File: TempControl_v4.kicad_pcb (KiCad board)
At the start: 2 copper layers, 57 x 38.1 mm, 42 parts, among them J1 LCD2, J2 PGM, J3 LCD1, J4 PWR, J5 Temp0, J6 Temp1, J7 AC, U1 PIC16(L)F88-I/P, U2 INA326, U3 INA326, U4 LM317_3PinPackage, U5 G3MB-202P

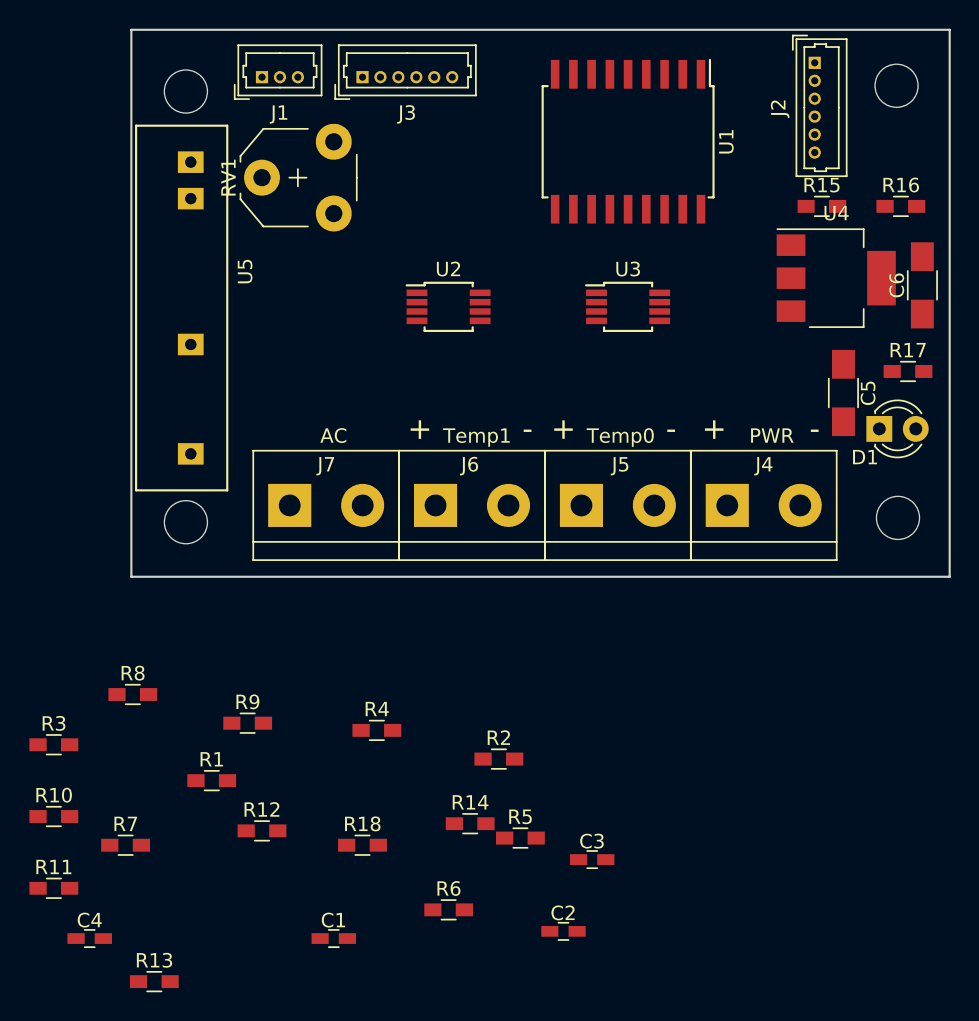
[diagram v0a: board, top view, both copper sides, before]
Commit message: Completed PCB layout
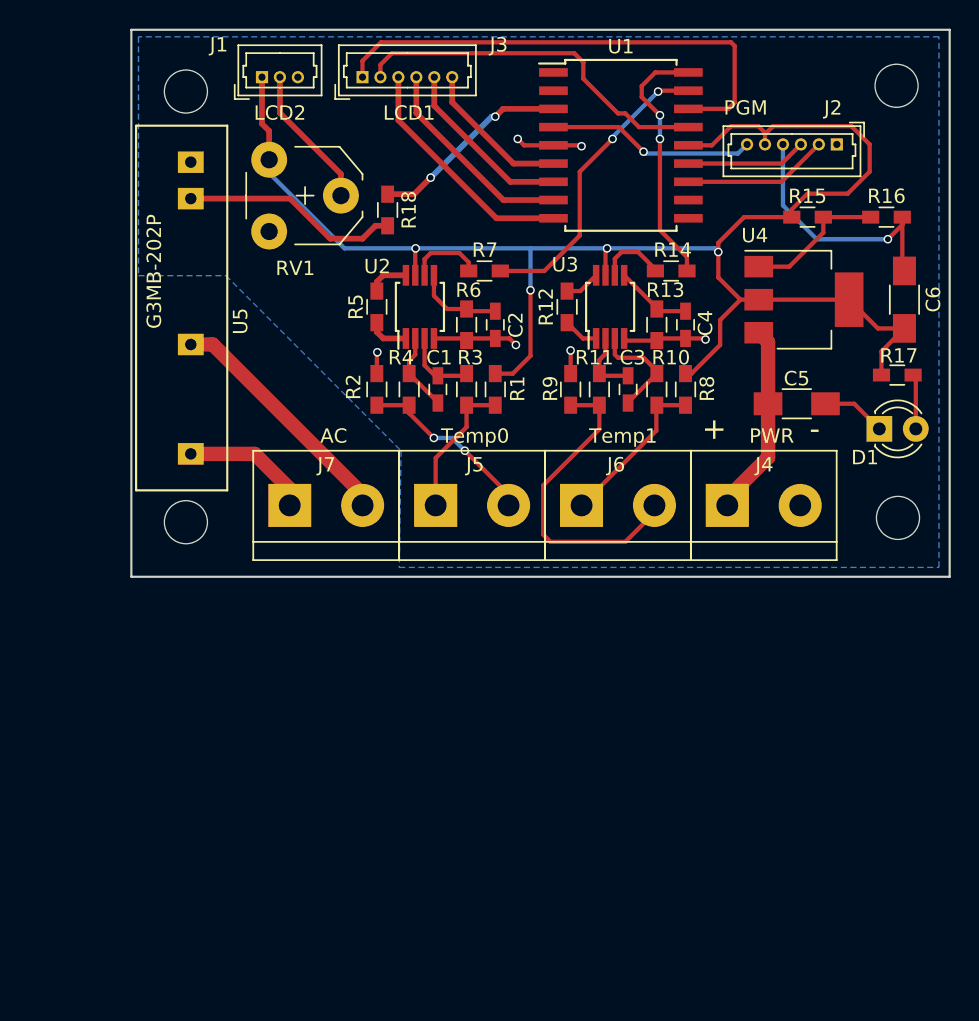
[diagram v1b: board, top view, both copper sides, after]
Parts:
- moved C4 59.6 mm to (166.5, 87.8), turned to 270 degrees
- moved R13 57.6 mm to (164.5, 87.8), turned to 270 degrees
- moved R11 51.5 mm to (160.5, 92.2), turned to 270 degrees
- moved R10 51.5 mm to (164.5, 92.2), turned to 270 degrees
- moved R7 47.2 mm to (152.5, 84.0), turned to 180 degrees
- moved R18 44.3 mm to (145.8, 79.8), turned to 90 degrees
- moved R8 44.0 mm to (166.5, 92.2), turned to 90 degrees
- moved C2 42.5 mm to (153.2, 87.8), turned to 270 degrees
- moved R12 42.2 mm to (158.2, 86.5), turned to 90 degrees
- moved R14 41.0 mm to (165.5, 84.0), turned to 180 degrees
- moved R6 40.8 mm to (151.2, 87.8), turned to 270 degrees
- moved C1 38.9 mm to (149.2, 92.2), turned to 270 degrees
- moved R5 38.3 mm to (145.0, 86.5), turned to 90 degrees
- moved R3 37.9 mm to (151.2, 92.2), turned to 270 degrees
- moved R1 33.7 mm to (153.2, 92.2), turned to 90 degrees
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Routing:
- net +5V: track 0.00 -> 112.2 mm, vias 0 -> 4
- net GND: track 0.00 -> 42.4 mm, vias 0 -> 7
- net Net-(J3-Pad1): track 0.00 -> 35.1 mm
- net Net-(J3-Pad2): track 0.00 -> 25.4 mm
- net /PT100_amp2/PT100_min: track 0.00 -> 21.9 mm
- net /PT100_amp/amp_out: track 0.00 -> 21.2 mm, vias 0 -> 2
- net /PT100_amp2/amp_out: track 0.00 -> 17.8 mm, vias 0 -> 2
- net /Relais/AC2_out: track 0.00 -> 17.1 mm
- net Net-(J3-Pad3): track 0.00 -> 16.6 mm
- net Net-(R18-Pad1): track 0.00 -> 15.2 mm
- net Net-(J3-Pad4): track 0.00 -> 14.6 mm
- net /PIC_VPP: track 0.00 -> 14.5 mm, vias 0 -> 1
- net /Power_supply/PWR_pos: track 0.00 -> 14.4 mm
- net /Relais/relais_trig: track 0.00 -> 14.0 mm, vias 0 -> 2
- net /PT100_amp/PT100_min: track 0.00 -> 13.1 mm, vias 0 -> 2
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- added copper zone on B.Cu, net GND
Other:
- net class Default: trace_width 0.25 -> 0.3
- net class High Voltage added: clearance 1.5, trace_width 1, via_dia 0.8, via_drill 0.6
- net class Power added: clearance 0.5, trace_width 1, via_dia 0.8, via_drill 0.6

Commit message: Added logo to PCB
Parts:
- added G***: LOGO, Graphics:Mountain_logo, B.Cu at (156.8, 82.2)
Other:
- board text added: "TempControl v4-Nov '17"

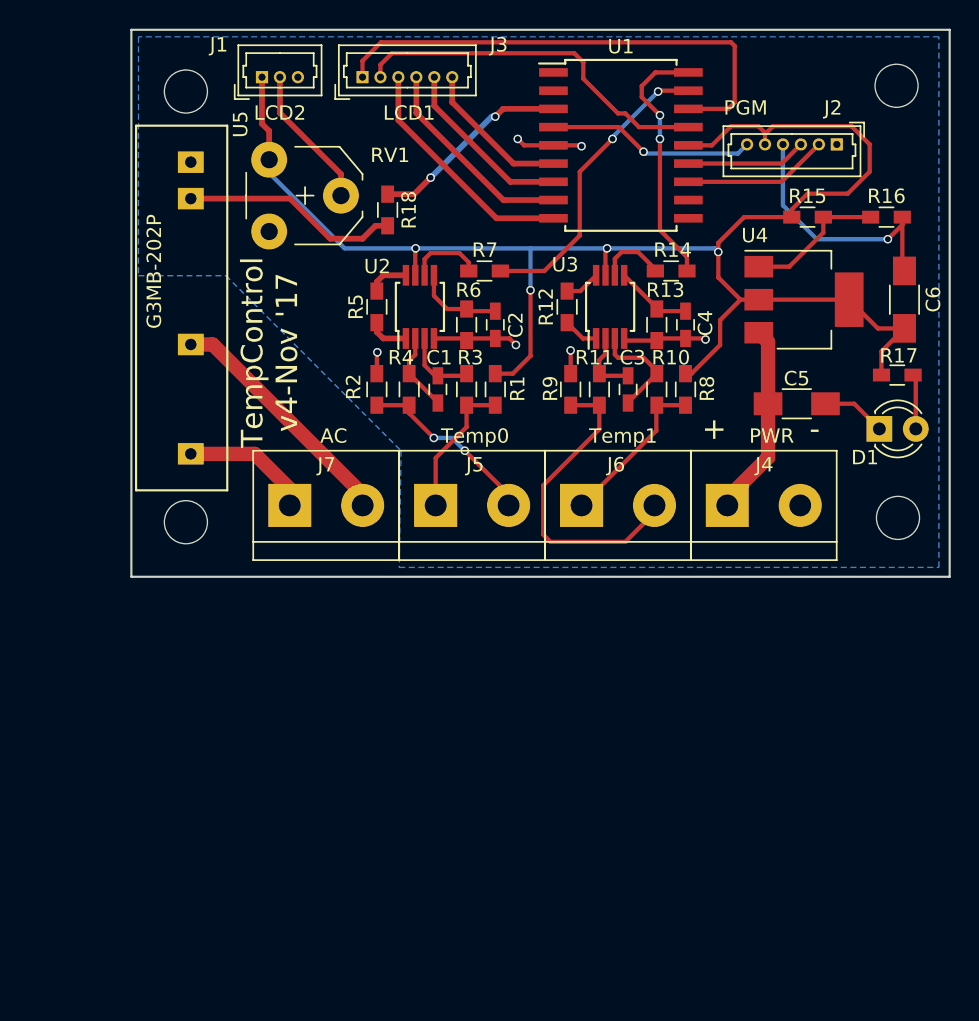
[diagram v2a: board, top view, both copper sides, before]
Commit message: Change from PT100 to thermistor
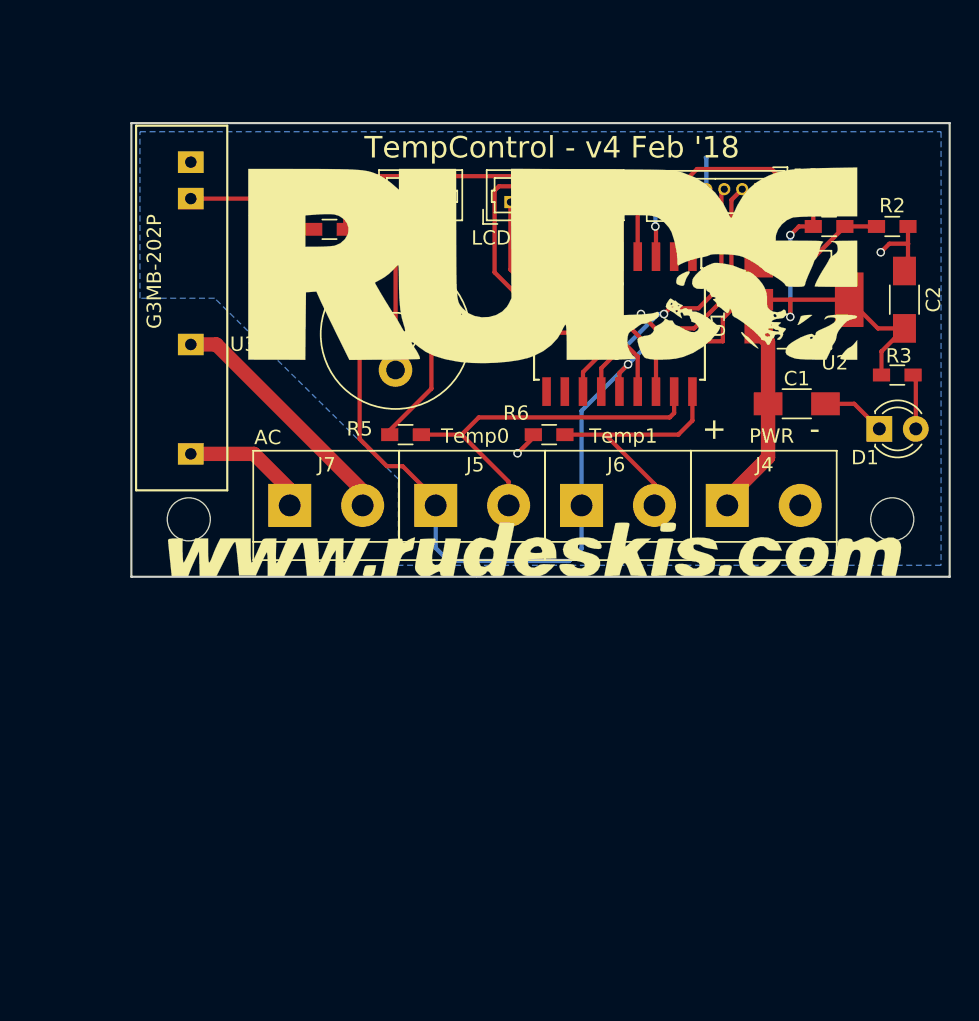
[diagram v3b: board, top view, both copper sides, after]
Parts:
- removed the C1 at (149.2, 92.2)
- removed the C2 at (153.2, 87.8)
- removed C3: 470nF, Capacitors_SMD:C_0603_HandSoldering
- removed C4: 500pF, Capacitors_SMD:C_0603_HandSoldering
- removed the R1 at (153.2, 92.2)
- removed R10, R11, R8, R9: 2.2k, Resistors_SMD:R_0603_HandSoldering
- removed R12: 20k, Resistors_SMD:R_0603_HandSoldering
- removed R13: 200k, Resistors_SMD:R_0603_HandSoldering
- removed R14, R7: 100, Resistors_SMD:R_0603_HandSoldering
- removed the R2 at (145.0, 92.2)
- removed the R3 at (151.2, 92.2)
- removed the R4 at (147.2, 92.2)
- removed the REF** at (181.3, 101.2)
- removed the REF** at (181.2, 71.1)
- removed the REF** at (131.7, 71.5)
- removed the REF** at (131.7, 101.5)
- removed the U2 at (148.0, 86.5)
- removed the U3 at (161.2, 86.5)
- added REF**: MountingHole_3mm, Mounting_Holes:MountingHole_3mm, F.Cu at (180.9, 101.3)
- added REF**: MountingHole_3mm, Mounting_Holes:MountingHole_3mm, F.Cu at (131.9, 101.3)
- G***: moved to F.Cu
- R5: value 20k -> 100k
- R6: value 200k -> 100k
- RV1: footprint Potentiometers:Potentiometer_Trimmer_VishaySpectrol_Econtrim-Type36M -> Potentiometers:Potentiometer_Trimmer_Piher_PT-10v5_Horizontal_Px5.0mm_Py5.0mm
- moved J3 13.5 mm to (154.3, 79.2)
- moved J1 13.1 mm to (146.8, 79.2)
- moved U1 12.5 mm to (161.9, 87.7), turned to 270 degrees
- moved RV1 11.5 mm to (143.8, 85.9)
- moved R6 9.57 mm to (157.0, 95.4), turned to 180 degrees
- moved R5 9.12 mm to (147.0, 95.4), turned to 180 degrees
- moved G*** 6.83 mm to (156.7, 89.0), turned to 0 degrees
- moved J2 6.18 mm to (171.7, 78.3)
- moved R4 4.27 mm to (141.7, 81.1), turned to 0 degrees
- moved R1 1.63 mm to (176.5, 80.9)
- moved R2 0.76 mm to (180.9, 80.9)
- renumbered C5 to C1, C6 to C2, R15 to R1, R16 to R2, R17 to R3, R18 to R4, U4 to U2, U5 to U3
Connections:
- J2 pad 1: Net-(J2-Pad1) -> (no net)
- J5 pad 1: /PT100_amp/PT100_pos -> +5V
- J5 pad 2: /PT100_amp/PT100_min -> /Thermistor0/Thermistor_2
- J6 pad 1: /PT100_amp2/PT100_pos -> +5V
- J6 pad 2: /PT100_amp2/PT100_min -> /Thermistor1/Thermistor_2
- R5 pad 1: Net-(R5-Pad1) -> /Thermistor0/Thermistor_2
- R5 pad 2: Net-(R5-Pad2) -> GND
- R6 pad 1: Net-(C2-Pad1) -> /Thermistor1/Thermistor_2
- U1 pad 1: Net-(U1-Pad1) -> (no net)
- U1 pad 10: Net-(U1-Pad10) -> (no net)
- U1 pad 11: Net-(U1-Pad11) -> (no net)
- U1 pad 17: /PT100_amp/amp_out -> /Thermistor0/Thermistor_2
- U1 pad 18: /PT100_amp2/amp_out -> /Thermistor1/Thermistor_2
- U1 pad 2: Net-(U1-Pad2) -> (no net)
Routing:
- net /Thermistor0/Thermistor_2: track 0.00 -> 27.9 mm
- net /PT100_amp2/PT100_min: track 21.9 -> 0.00 mm
- net /PT100_amp/amp_out: track 21.2 -> 0.00 mm, vias 2 -> 0
- net /Thermistor1/Thermistor_2: track 0.00 -> 18.2 mm
- net /PT100_amp2/amp_out: track 17.8 -> 0.00 mm, vias 2 -> 0
- net Net-(J3-Pad1): track 35.1 -> 19.9 mm
- net /Relais/relais_trig: track 14.0 -> 28.6 mm
- net GND: track 42.4 -> 28.2 mm, vias 7 -> 3
- net /PT100_amp/PT100_min: track 13.1 -> 0.00 mm, vias 2 -> 0
- net Net-(J3-Pad3): track 16.6 -> 3.81 mm
- net /PIC_PGC: track 10.2 -> 22.3 mm, vias 0 -> 2
- net /PT100_amp2/PT100_pos: track 11.2 -> 0.00 mm
- net /PIC_PGD: track 8.39 -> 19.5 mm, vias 0 -> 2
- net Net-(J3-Pad4): track 14.6 -> 3.82 mm
- net /PT100_amp/PT100_pos: track 9.87 -> 0.00 mm
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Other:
- board size 57 x 38.1 mm -> 57 x 31.6 mm
- board text added: "TempControl - v4 Feb '18"
- board text removed: "TempControl v4-Nov '17"

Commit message: Moved logo to bottom side
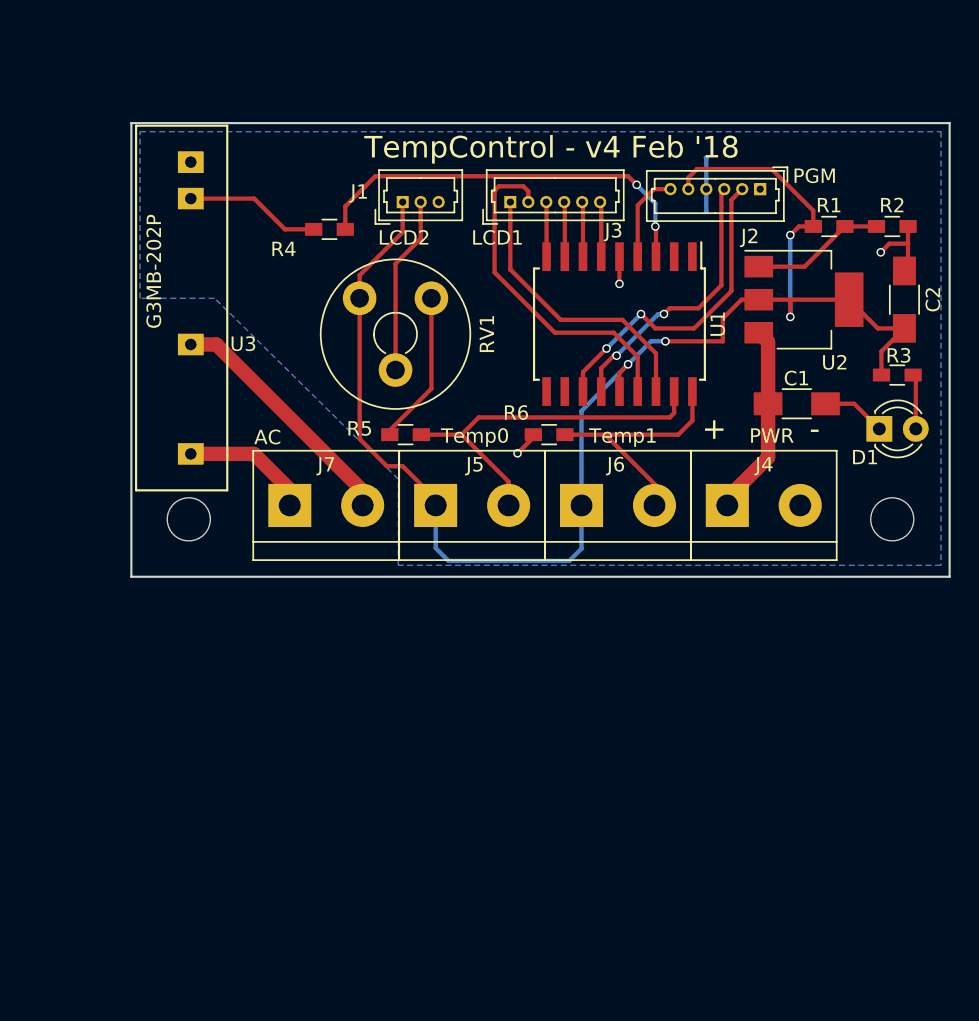
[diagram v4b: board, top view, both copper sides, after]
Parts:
- G***: moved to B.Cu
- moved G*** 1.30 mm to (155.4, 89.0), turned to 180 degrees
